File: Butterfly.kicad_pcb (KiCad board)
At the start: 2 copper layers, 93.1 x 65.5 mm, 29 parts, among them J1 Conn_02x03_Odd_Even, J2 USB_A, J3 Conn_01x02, U1 ATTINY85-20PU

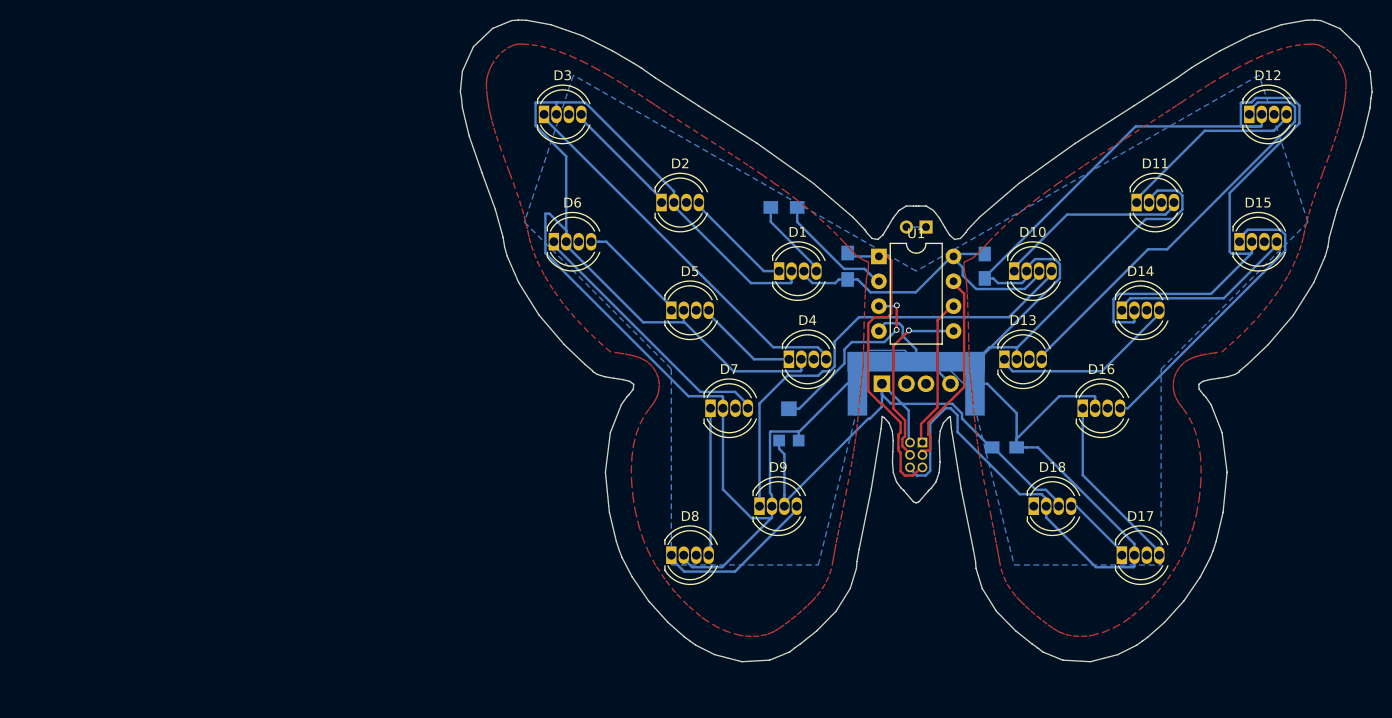
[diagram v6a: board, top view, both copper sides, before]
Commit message: Propagate new footprint associations to layout.
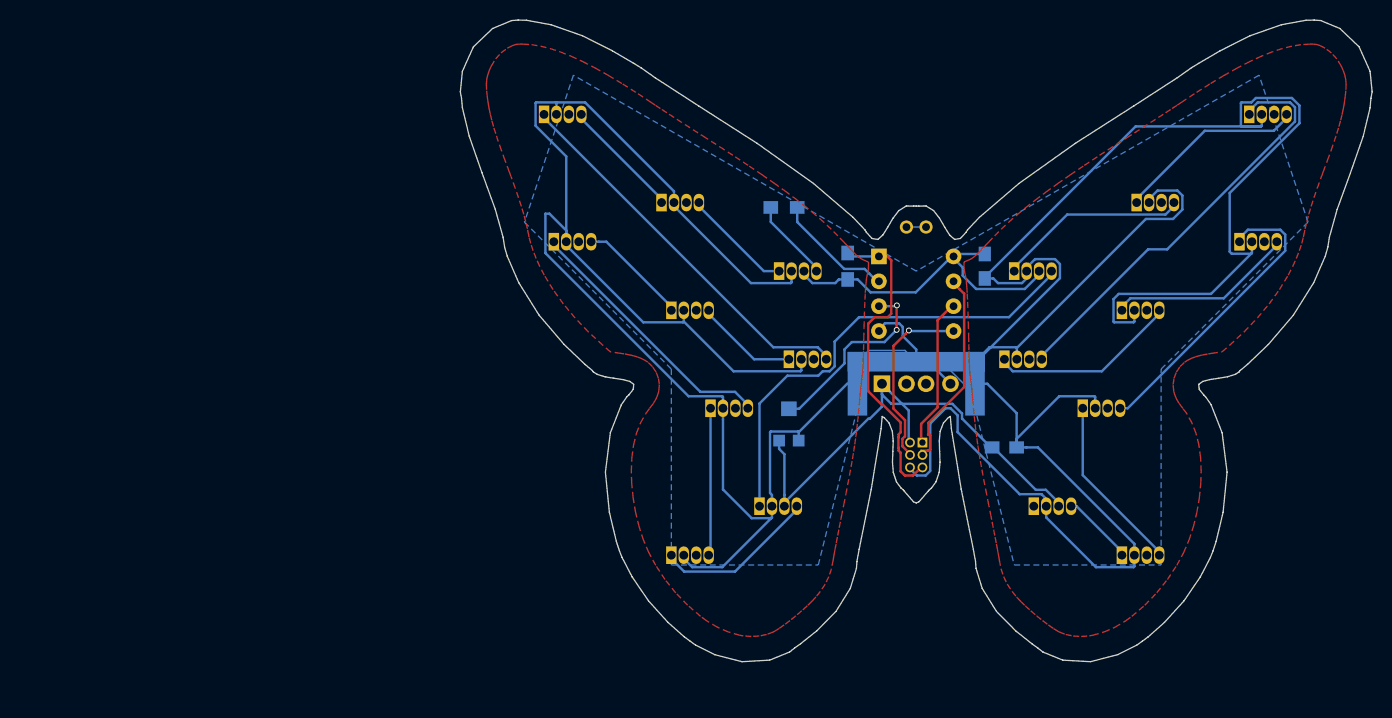
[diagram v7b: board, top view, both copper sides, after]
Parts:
- D1, D10, D11, D12, D13, D14, D15, D16, D17, D18, D2, D3, D4, D5, D6, D7, D8, D9: footprint LEDs:LED_D5.0mm-4 -> myLibrary:LED_D5.0mm-4
- J3: footprint Pin_Headers:Pin_Header_Straight_1x02_Pitch2.00mm -> myLibrary:Antennae
- U1: footprint Housings_DIP:DIP-8_W7.62mm -> myLibrary:DIP-8_W7.62mm

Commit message: Flip board over, so back is front.
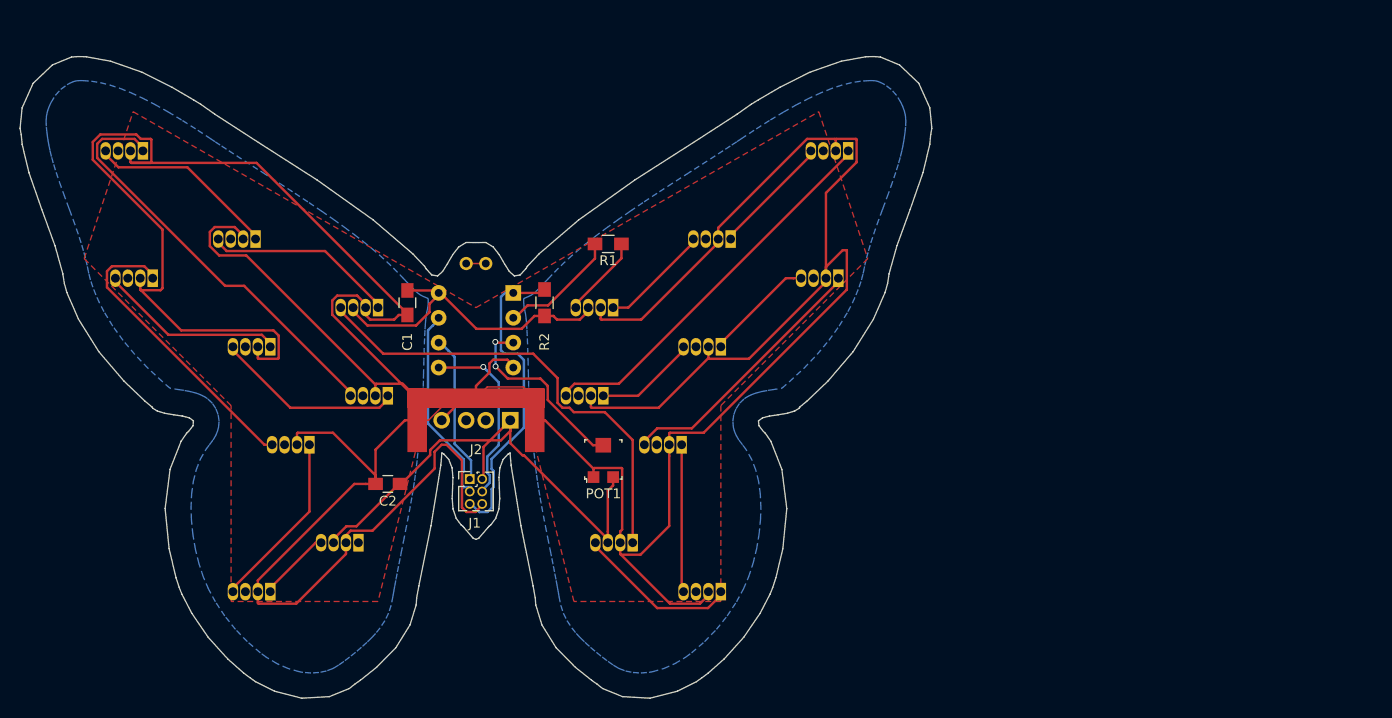
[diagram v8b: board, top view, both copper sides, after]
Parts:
- C1, C2, J1, J2, J3, POT1, R1, R2: moved to F.Cu
- D1, D10, D11, D12, D13, D14, D15, D16, D17, D18, D2, D3, D4, D5, D6, D7, D8, D9, G*** (x2), U1: moved to B.Cu
- moved D12 113.0 mm to (66.1, 82.7), turned to 180 degrees
- moved D15 111.0 mm to (67.1, 95.7), turned to 180 degrees
- moved G*** 92.0 mm to (76.6, 105.2), turned to 180 degrees
- moved D11 90.0 mm to (77.6, 91.7), turned to 180 degrees
- moved D14 87.0 mm to (79.1, 102.7), turned to 180 degrees
- moved D17 87.0 mm to (79.1, 127.7), turned to 180 degrees
- moved D16 79.0 mm to (83.1, 112.7), turned to 180 degrees
- moved D18 69.0 mm to (88.1, 122.7), turned to 180 degrees
- moved D10 65.1 mm to (90.1, 98.7), turned to 180 degrees
- moved C2 63.1 mm to (91.1, 116.7), turned to 180 degrees
- moved D13 63.1 mm to (91.1, 107.7), turned to 180 degrees
- moved C1 59.1 mm to (93.1, 98.2)
- moved J3 47.1 mm to (99.1, 94.2)
- moved J1 46.4 mm to (99.4, 116.2), turned to 0 degrees
- moved J2 45.1 mm to (100.1, 110.2), turned to 0 degrees
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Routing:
- added copper zone on B.Cu, net +5V
- added copper zone on F.Cu, net GND
- removed copper zone on F.Cu, net +5V
- removed copper zone on B.Cu, net GND
